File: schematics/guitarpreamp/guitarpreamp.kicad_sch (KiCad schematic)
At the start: 60 parts, among them J1 10k Pot, J2 Conn_01x07_Female, J3 Phones, Line Out, Line In, Mi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, U1 9V Linear Regulator, U2 TL074, U3 5V Linear Regulator, U4 3.3V Digital, U5 3.3V Analog, U6 WM8731SEDS, Y1 12.288MHz

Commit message: work on schematics
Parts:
- removed U2: TL074, symbol Amplifier_Operational:TL074
- added J4: Power Input, Connector_PinHeader_2.54mm:PinHeader_1x02_P2.54mm_Vertical, symbol Connector:Conn_01x02_Female
- added R19, R20: 10k, Resistor_SMD:R_0603_1608Metric_Pad0.98x0.95mm_HandSolder, symbol Device:R
- added U2: TL072, Package_SO:SOIC-8_3.9x4.9mm_P1.27mm, symbol Amplifier_Operational:TL072
- C1, C12, C13, C16, C17, C18, C19, C2, C22, C23, C24, C29, C3, C4, C5, C6, C7, C9: footprint (none) -> Capacitor_SMD:CP_Elec_4x4.5
- C10, C11: value ?pF -> 22pF; footprint (none) -> Capacitor_SMD:C_0603_1608Metric_Pad1.08x0.95mm_HandSolder
- C14, C15, C20, C21, C25: footprint (none) -> Capacitor_SMD:C_1210_3225Metric_Pad1.33x2.70mm_HandSolder
- C26, C27, C28, C8: footprint (none) -> Capacitor_SMD:C_0603_1608Metric_Pad1.08x0.95mm_HandSolder
- C30, C31: footprint (none) -> Capacitor_SMD:CP_Elec_6.3x7.7
- GuitarInput1: footprint (none) -> Connector_PinHeader_2.54mm:PinHeader_1x02_P2.54mm_Vertical
- J1: footprint (none) -> Connector_PinHeader_2.54mm:PinHeader_1x03_P2.54mm_Vertical
- J2: footprint (none) -> Connector_PinHeader_2.54mm:PinHeader_1x07_P2.54mm_Vertical
- J3: footprint (none) -> Connector_PinHeader_2.54mm:PinHeader_1x06_P2.54mm_Vertical
- R1, R10, R11, R12, R13, R14, R15, R16, R17, R18, R2, R3, R4, R5, R6, R7, R8, R9: footprint (none) -> Resistor_SMD:R_0603_1608Metric_Pad0.98x0.95mm_HandSolder
- U6: footprint Package_SO:SSOP-28_5.3x10.2mm_P0.65mm -> Package_DFN_QFN:QFN-28-1EP_5x5mm_P0.5mm_EP3.75x3.75mm
- Y1: footprint (none) -> Crystal:Crystal_SMD_HC49-SD_HandSoldering
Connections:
- net +12V: now also J4.2 (Pin_2)
- net +9V: now also U2.8 (V+)
- net GND: now also J4.1 (Pin_1), U2.4 (V-)
- net at C6.1, R4.1: now also U2.5 (+)
- net at C8.1, R3.2, R5.2: now also U2.6 (-)
- net at C8.2, C9.1, R5.1: now also U2.7
- net at C12.1, C13.1, C14.1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: now also R19.2, R20.2
- net at C5.1, R1.1, R2.2: now also U2.3 (+)
- net at R4.2: now also U2.1, U2.2 (-)
- net at J2.3 (Pin_3), U6.23 (SDIN): now also R19.1
- net at J2.2 (Pin_2), U6.24 (SCLK): now also R20.1
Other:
- moved on the sheet: C10, C11, C12, C13, C14, C15, C16, C17, C18, C19, C20, C21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

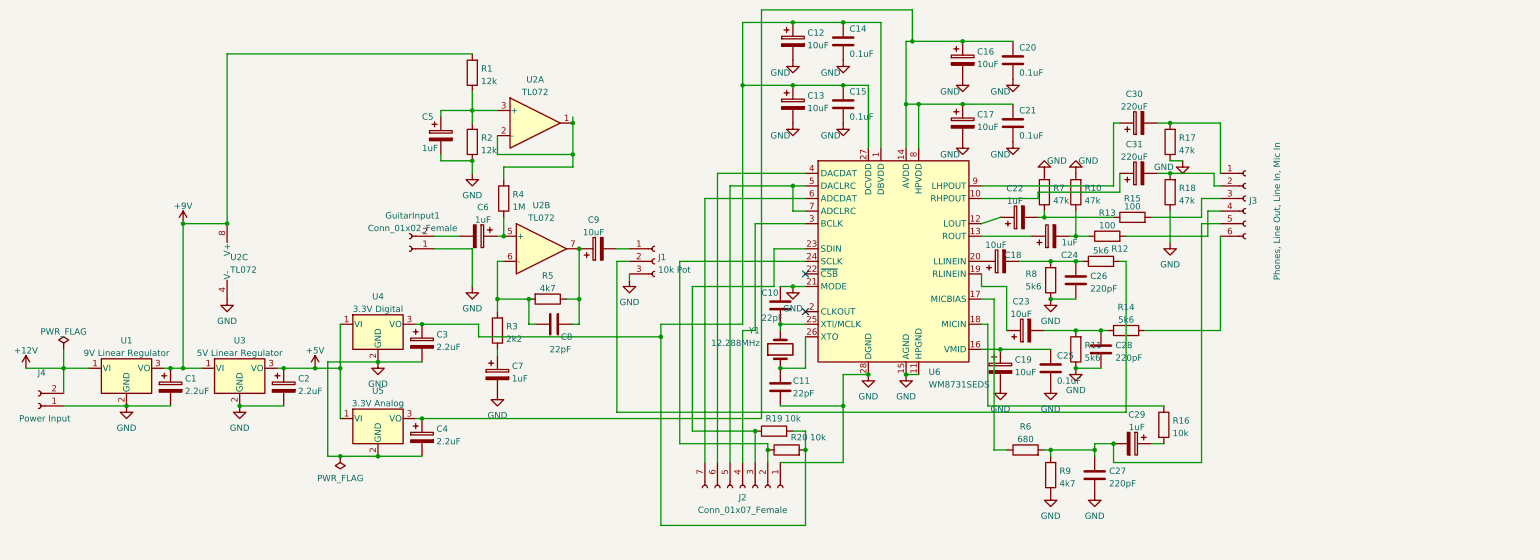
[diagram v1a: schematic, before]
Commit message: schematics
* moved fritzing schematics to schematics folder
* updated pcb
* adapted gitignore
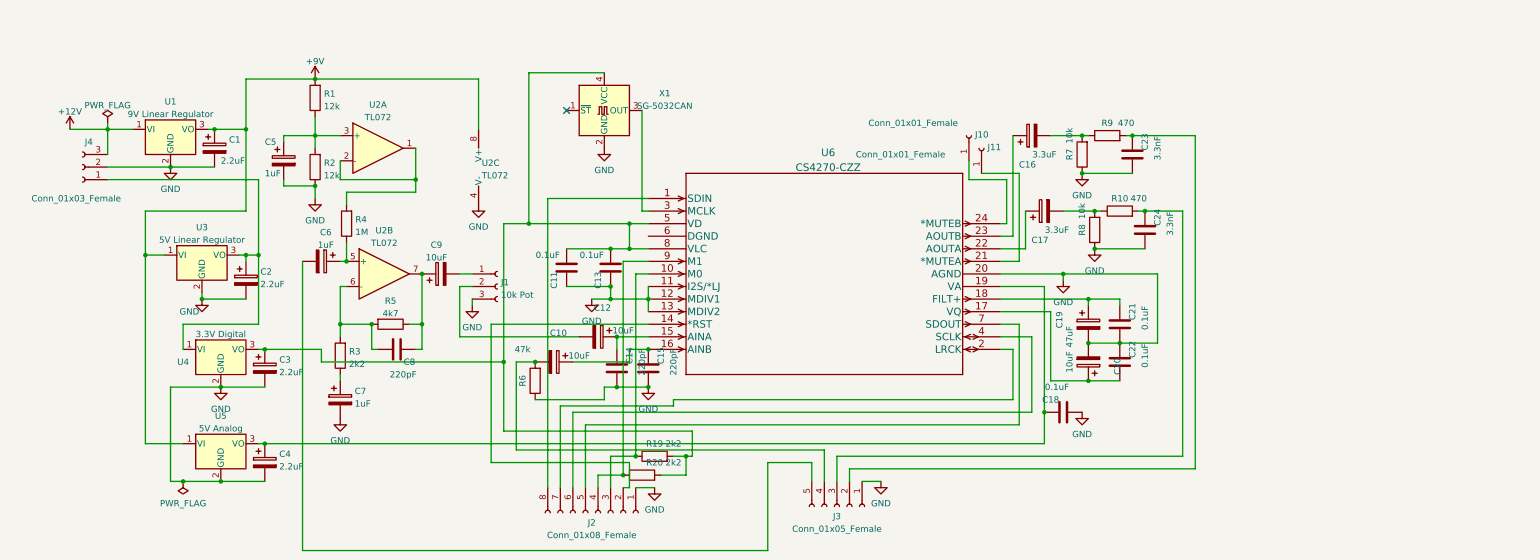
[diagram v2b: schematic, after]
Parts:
- removed C10: 22pF, Capacitor_SMD:C_0603_1608Metric_Pad1.08x0.95mm_HandSolder, symbol Device:C
- removed C13, C18, C23: 10uF, Capacitor_SMD:CP_Elec_4x4.5, symbol Device:C_Polarized
- removed C20, C25: 0.1uF, Capacitor_SMD:C_1210_3225Metric_Pad1.33x2.70mm_HandSolder, symbol Device:C
- removed C22, C24, C29: 1uF, Capacitor_SMD:CP_Elec_4x4.5, symbol Device:C_Polarized
- removed C26, C27, C28: 220pF, Capacitor_SMD:C_0603_1608Metric_Pad1.08x0.95mm_HandSolder, symbol Device:C
- removed C30, C31: 220uF, Capacitor_SMD:CP_Elec_6.3x7.7, symbol Device:C_Polarized
- removed GuitarInput1: Conn_01x02_Female, Connector_PinHeader_2.54mm:PinHeader_1x02_P2.54mm_Vertical, symbol Connector:Conn_01x02_Female
- removed J2: Conn_01x07_Female, Connector_PinHeader_2.54mm:PinHeader_1x07_P2.54mm_Vertical, symbol Connector:Conn_01x07_Female
- removed J3: Phones, Line Out, Line In, Mic In, Connector_PinHeader_2.54mm:PinHeader_1x06_P2.54mm_Vertical, symbol Connector:Conn_01x06_Female
- removed J4: Power Input, Connector_PinHeader_2.54mm:PinHeader_1x02_P2.54mm_Vertical, symbol Connector:Conn_01x02_Female
- removed R11, R12, R14: 5k6, Resistor_SMD:R_0603_1608Metric_Pad0.98x0.95mm_HandSolder, symbol Device:R
- removed R13, R15: 100, Resistor_SMD:R_0603_1608Metric_Pad0.98x0.95mm_HandSolder, symbol Device:R
- removed R16: 10k, Resistor_SMD:R_0603_1608Metric_Pad0.98x0.95mm_HandSolder, symbol Device:R
- removed R17, R18: 47k, Resistor_SMD:R_0603_1608Metric_Pad0.98x0.95mm_HandSolder, symbol Device:R
- removed U6: WM8731SEDS, Package_DFN_QFN:QFN-28-1EP_5x5mm_P0.5mm_EP3.75x3.75mm, symbol Audio:WM8731SEDS
- removed Y1: 12.288MHz, Crystal:Crystal_SMD_HC49-SD_HandSoldering, symbol Device:Crystal
- added C10, C20: 10uF, Capacitor_SMD:CP_Elec_4x4.5, symbol Device:C_Polarized
- added C13, C18, C22: 0.1uF, Capacitor_SMD:C_1210_3225Metric_Pad1.33x2.70mm_HandSolder, symbol Device:C
- added C23, C24: 3.3nF, Capacitor_SMD:C_0805_2012Metric_Pad1.18x1.45mm_HandSolder, symbol Device:C
- added J10, J11: Conn_01x01_Female, Connector_Pin:Pin_D0.7mm_L6.5mm_W1.8mm_FlatFork, symbol Connector:Conn_01x01_Female
- added J2: Conn_01x08_Female, Connector_PinHeader_2.54mm:PinHeader_1x08_P2.54mm_Vertical, symbol Connector:Conn_01x08_Female
- added J3: Conn_01x05_Female, Connector_PinHeader_2.54mm:PinHeader_1x05_P2.54mm_Vertical, symbol Connector:Conn_01x05_Female
- added J4: Conn_01x03_Female, Connector_PinHeader_2.54mm:PinHeader_1x03_P2.54mm_Vertical, symbol Connector:Conn_01x03_Female
- added U6: CS4270-CZZ, Package_SO:TSSOP-24_4.4x7.8mm_P0.65mm, symbol 2022-10-31_07-27-24:CS4270-CZZ
- added X1: SG-5032CAN, Oscillator:Oscillator_SMD_SeikoEpson_SG8002CA-4Pin_7.0x5.0mm_HandSoldering, symbol Oscillator:SG-5032CAN
- C11: value 22pF -> 0.1uF; footprint Capacitor_SMD:C_0603_1608Metric_Pad1.08x0.95mm_HandSolder -> Capacitor_SMD:C_1210_3225Metric_Pad1.33x2.70mm_HandSolder
- C14, C15: value 0.1uF -> 220pF; footprint Capacitor_SMD:C_1210_3225Metric_Pad1.33x2.70mm_HandSolder -> Capacitor_SMD:C_0603_1608Metric_Pad1.08x0.95mm_HandSolder
- C16, C17: value 10uF -> 3.3uF
- C19: value 10uF -> 47uF
- C8: value 22pF -> 220pF
- R10: value 47k -> 470
- R19, R20: value 10k -> 2k2
- R6: value 680 -> 47k
- R7: value 47k -> 10k
- R8: value 5k6 -> 10k
- R9: value 4k7 -> 470
- U4: footprint Package_TO_SOT_SMD:TO-252-2 -> Package_TO_SOT_SMD:TSOT-23-5_HandSoldering
- U5: value 3.3V Analog -> 5V Analog; footprint Package_TO_SOT_SMD:TO-252-2 -> Package_TO_SOT_SMD:TSOT-23-5_HandSoldering
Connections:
- net +12V: now also J4.3 (Pin_3)
- net +9V: now also U5.1 (VI)
- net GND: now also C14.1, C15.1, C21.1, R6.1, R7.1, C13.2, C18.1, C20.2, C22.2, C23.1, C24.1, J2.1 (Pin_1), J3.1 (Pin_1), J4.2 (Pin_2), U6.11 (I2S/*LJ), U6.12 (MDIV1), U6.13 (MDIV2), U6.20 (AGND), X1.2 (GND); no longer C12.2, C14.2, C15.2, C16.2, C17.2, C21.2, R10.2, R7.2, R9.1
- net at C11.1: now also C3.1, R19.2, R20.2, U4.3 (VO), C13.1, U6.5 (VD), U6.8 (VLC), X1.4 (VCC)
- net at R6.2: now also C10.2, J3.4 (Pin_4); no longer R9.2
- net at R10.1: now also C17.2, R8.2
- net at J1.2 (Pin_2): now also C12.2
- net at R20.1: now also J2.4 (Pin_4), U6.9 (M1)
- net at C6.2: now also J3.5 (Pin_5)
- net at C19.1: now also C21.2, U6.18 (FILT+)
- net at R19.1: now also J2.3 (Pin_3), U6.10 (M0)
- net +5V: no longer names the net of C2.1, U3.3 (VO), U4.1 (VI)
- net +5V: now also J4.1 (Pin_1); no longer U5.1 (VI)
- new net: C17.1, U6.22 (AOUTA)
- new net: C20.1, C22.1, U6.17 (VQ)
- new net: C12.1, C14.2, U6.15 (AINA)
- new net: C18.2, C4.1, U5.3 (VO), U6.19 (VA)
- new net: C24.2, J3.3 (Pin_3), R10.2
- new net: C10.1, C15.2, U6.16 (AINB)
- new net: J2.8 (Pin_8), U6.1 (SDIN)
- new net: J2.2 (Pin_2), U6.14 (*RST)
- new net: J2.7 (Pin_7), U6.2 (LRCK)
- new net: J11.1 (Pin_1), U6.21 (*MUTEA)
- new net: C16.1, U6.23 (AOUTB)
- new net: J10.1 (Pin_1), U6.24 (*MUTEB)
- new net: U6.3 (MCLK), X1.3 (OUT)
- new net: J2.6 (Pin_6), U6.4 (SCLK)
- new net: J2.5 (Pin_5), U6.7 (SDOUT)
- new net: C16.2, R7.2, R9.1
- new net: C23.2, J3.2 (Pin_2), R9.2
- no-connect marks 2 -> 1
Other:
- moved on the sheet: C1, C2, C3, C4, C5, C6, C7, C8, C9, J1, R1, R19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

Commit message: corrected some design mistakes
* connected oscillator enable to reset
* attached DGND
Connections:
- net GND: now also U6.6 (DGND)
- net at J2.2 (Pin_2), U6.14 (*RST): now also X1.1 (~{ST})
- no-connect marks 1 -> 0
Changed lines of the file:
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@@
   (junction (at 88.9 85.09) (diameter 0) (color 0 0 0 0)
   )
+  (junction (at 121.92 85.09) (diameter 0) (color 0 0 0 0)
+  )
   (junction (at 63.5 71.12) (diameter 0) (color 0 0 0 0)
   )
@@
   (junction (at 77.47 35.56) (diameter 0) (color 0 0 0 0)
   )
-  (no_connect (at 128.27 41.91))
   (wire (pts (xy 139.7 72.39) (xy 144.78 72.39))
     (stroke (width 0) (type default) (color 0 0 0 0))
@@
     (stroke (width 0) (type default) (color 0 0 0 0))
   )
+  (wire (pts (xy 134.62 67.31) (xy 144.78 67.31))
+    (stroke (width 0) (type default) (color 0 0 0 0))
+  )
   (wire (pts (xy 97.79 49.53) (xy 97.79 55.88))
     (stroke (width 0) (type default) (color 0 0 0 0))
@@
     (stroke (width 0) (type default) (color 0 0 0 0))
   )
+  (wire (pts (xy 121.92 41.91) (xy 121.92 85.09))
+    (stroke (width 0) (type default) (color 0 0 0 0))
+  )
   (wire (pts (xy 82.55 85.09) (xy 82.55 87.63))
     (stroke (width 0) (type default) (color 0 0 0 0))
@@
     (stroke (width 0) (type default) (color 0 0 0 0))
   )
+  (wire (pts (xy 121.92 85.09) (xy 144.78 85.09))
+    (stroke (width 0) (type default) (color 0 0 0 0))
+  )
   (wire (pts (xy 78.74 92.71) (xy 115.57 92.71))
     (stroke (width 0) (type default) (color 0 0 0 0))
@@
     (stroke (width 0) (type default) (color 0 0 0 0))
   )
-  (wire (pts (xy 113.03 85.09) (xy 144.78 85.09))
+  (wire (pts (xy 113.03 85.09) (xy 121.92 85.09))
     (stroke (width 0) (type default) (color 0 0 0 0))
   )
@@
   )
   (wire (pts (xy 63.5 45.72) (xy 63.5 35.56))
+    (stroke (width 0) (type default) (color 0 0 0 0))
+  )
+  (wire (pts (xy 128.27 41.91) (xy 121.92 41.91))
     (stroke (width 0) (type default) (color 0 0 0 0))
   )
@@
     (pin "2")
   )
+  (symbol (lib_id "power:GND") (at 134.62 67.31 270) (unit 1)
+    (in_bom yes) (on_board yes) (fields_autoplaced)
+    (property "Reference" "#PWR0116" (id 0) (at 128.27 67.31 0)
+      (effects (font (size 1.27 1.27)) hide)
+    )
+    (property "Value" "GND" (id 1) (at 131.4451 67.7438 90)
+      (effects (font (size 1.27 1.27)) (justify right))
+    )
+    (property "Footprint" "" (id 2) (at 134.62 67.31 0)
+      (effects (font (size 1.27 1.27)) hide)
+    )
+    (property "Datasheet" "" (id 3) (at 134.62 67.31 0)
+      (effects (font (size 1.27 1.27)) hide)
+    )
+    (pin "1")
+  )
   (symbol (lib_id "Device:R") (at 146.05 111.76 90) (unit 1)
     (in_bom yes) (on_board yes)
@@
       (reference "#PWR0115") (unit 1) (value "GND") (footprint "")
     )
+    (path "/957cba0c-9fde-4e24-888d-b1f289337beb"
+      (reference "#PWR0116") (unit 1) (value "GND") (footprint "")
+    )
     (path "/50a071a5-b567-4944-812b-66a65a33ff2d"

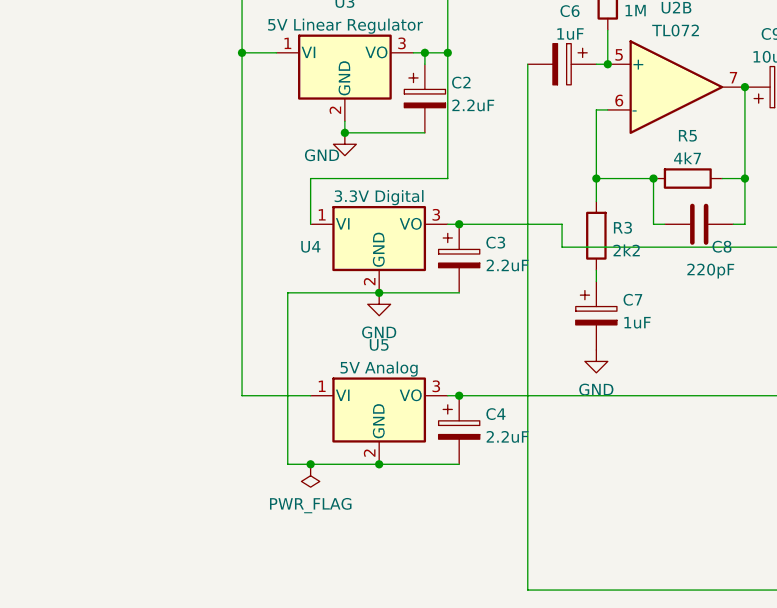
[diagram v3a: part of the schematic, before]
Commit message: changed regulators, added design fixes
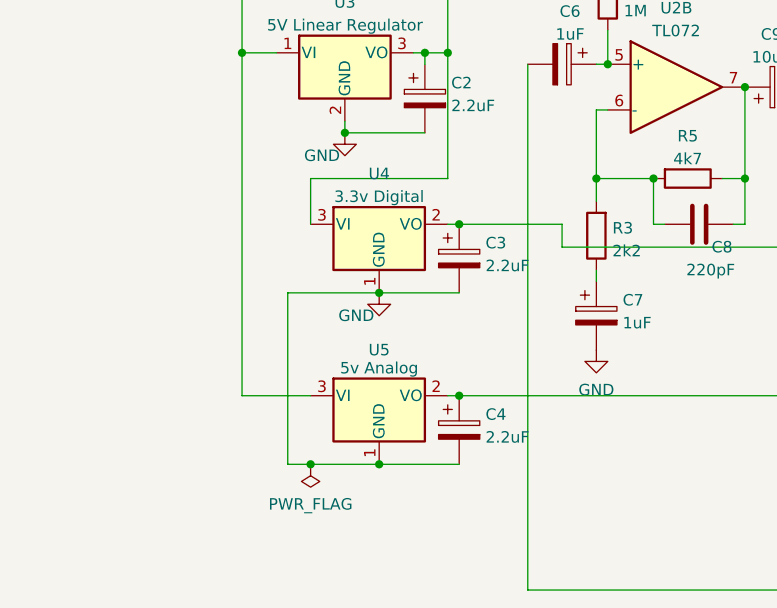
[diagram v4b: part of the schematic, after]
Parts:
- removed U4: 3.3V Digital, Package_TO_SOT_SMD:TSOT-23-5_HandSoldering, symbol Regulator_Linear:LM78M05_TO252
- removed U5: 5V Analog, Package_TO_SOT_SMD:TSOT-23-5_HandSoldering, symbol Regulator_Linear:LM78M05_TO252
- added U4: 3.3v Digital, Package_TO_SOT_SMD:SOT-23, symbol Regulator_Linear:MCP1700-1202E_SOT23
- added U5: 5v Analog, Package_TO_SOT_SMD:SOT-23, symbol Regulator_Linear:MCP1700-1202E_SOT23
- C19: footprint Capacitor_SMD:CP_Elec_4x4.5 -> Capacitor_SMD:CP_Elec_5x5.4
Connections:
- net +9V: now also U5.3 (VI)
- net GND: now also U4.1 (GND), U5.1 (GND)
- net at C18.2, C4.1, U6.19 (VA): now also U5.2 (VO)
- net at C11.1, C13.1, C3.1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: now also U4.2 (VO)
- net at C2.1, J4.1 (Pin_1), U3.3 (VO): now also U4.3 (VI)
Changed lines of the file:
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@@
 (kicad_sch (version 20211123) (generator eeschema)
   (paper "A4")
+  (junction (at 58.42 116.84) (diameter 0) (color 0 0 0 0)
+  )
   (junction (at 35.56 45.72) (diameter 0) (color 0 0 0 0)
   )
@@
   (junction (at 99.06 74.93) (diameter 0) (color 0 0 0 0)
   )
-  (junction (at 58.42 116.84) (diameter 0) (color 0 0 0 0)
-  )
   (junction (at 245.11 62.23) (diameter 0) (color 0 0 0 0)
   )
@@
     (stroke (width 0) (type default) (color 0 0 0 0))
   )
-  (wire (pts (xy 58.42 116.84) (xy 50.8 116.84))
+  (wire (pts (xy 50.8 116.84) (xy 58.42 116.84))
     (stroke (width 0) (type default) (color 0 0 0 0))
   )
@@
     (stroke (width 0) (type default) (color 0 0 0 0))
   )
+  (wire (pts (xy 58.42 116.84) (xy 67.31 116.84))
+    (stroke (width 0) (type default) (color 0 0 0 0))
+  )
   (wire (pts (xy 143.51 41.91) (xy 143.51 62.23))
     (stroke (width 0) (type default) (color 0 0 0 0))
@@
   )
   (wire (pts (xy 240.03 80.01) (xy 240.03 81.28))
-    (stroke (width 0) (type default) (color 0 0 0 0))
-  )
-  (wire (pts (xy 58.42 116.84) (xy 67.31 116.84))
     (stroke (width 0) (type default) (color 0 0 0 0))
   )
@@
     (pin "2")
   )
-  (symbol (lib_id "Regulator_Linear:LM78M05_TO252") (at 58.42 109.22 0) (unit 1)
-    (in_bom yes) (on_board yes) (fields_autoplaced)
-    (property "Reference" "U5" (id 0) (at 58.42 103.6152 0))
-    (property "Value" "5V Analog" (id 1) (at 58.42 106.1521 0))
-    (property "Footprint" "Package_TO_SOT_SMD:TSOT-23-5_HandSoldering" (id 2) (at 58.42 103.505 0)
-      (effects (font (size 1.27 1.27) italic) hide)
-    )
-    (property "Datasheet" "https://www.onsemi.com/pub/Collateral/MC78M00-D.PDF" (id 3) (at 58.42 110.49 0)
-      (effects (font (size 1.27 1.27)) hide)
-    )
-    (pin "1")
-    (pin "2")
-    (pin "3")
-  )
-  (symbol (lib_id "Regulator_Linear:LM78M05_TO252") (at 58.42 90.17 0) (unit 1)
-    (in_bom yes) (on_board yes)
-    (property "Reference" "U4" (id 0) (at 50.8 92.71 0))
-    (property "Value" "3.3V Digital" (id 1) (at 58.42 87.1021 0))
-    (property "Footprint" "Package_TO_SOT_SMD:TSOT-23-5_HandSoldering" (id 2) (at 58.42 84.455 0)
-      (effects (font (size 1.27 1.27) italic) hide)
-    )
-    (property "Datasheet" "https://www.onsemi.com/pub/Collateral/MC78M00-D.PDF" (id 3) (at 58.42 91.44 0)
-      (effects (font (size 1.27 1.27)) hide)
-    )
-    (pin "1")
-    (pin "2")
-    (pin "3")
-  )
   (symbol (lib_id "Device:C") (at 138.43 93.98 180) (unit 1)
     (in_bom yes) (on_board yes)
@@
     (pin "2")
   )
+  (symbol (lib_id "Regulator_Linear:MCP1700-1202E_SOT23") (at 58.42 90.17 0) (unit 1)
+    (in_bom yes) (on_board yes) (fields_autoplaced)
+    (property "Reference" "U4" (id 0) (at 58.42 84.5652 0))
+    (property "Value" "3.3v Digital" (id 1) (at 58.42 87.1021 0))
+    (property "Footprint" "Package_TO_SOT_SMD:SOT-23" (id 2) (at 58.42 84.455 0)
+      (effects (font (size 1.27 1.27)) hide)
+    )
+    (property "Datasheet" "http://ww1.microchip.com/downloads/en/DeviceDoc/20001826D.pdf" (id 3) (at 58.42 90.17 0)
+      (effects (font (size 1.27 1.27)) hide)
+    )
+    (pin "1")
+    (pin "2")
+    (pin "3")
+  )
   (symbol (lib_id "Device:C_Polarized") (at 125.73 92.71 270) (unit 1)
     (in_bom yes) (on_board yes)
@@
   )
   (symbol (lib_id "power:GND") (at 58.42 97.79 0) (unit 1)
-    (in_bom yes) (on_board yes) (fields_autoplaced)
+    (in_bom yes) (on_board yes)
     (property "Reference" "#PWR0101" (id 0) (at 58.42 104.14 0)
       (effects (font (size 1.27 1.27)) hide)
     )
-    (property "Value" "GND" (id 1) (at 58.42 102.2334 0))
+    (property "Value" "GND" (id 1) (at 55.88 100.33 0))
     (property "Footprint" "" (id 2) (at 58.42 97.79 0)
       (effects (font (size 1.27 1.27)) hide)
@@
     (pin "1")
   )
+  (symbol (lib_id "Regulator_Linear:MCP1700-1202E_SOT23") (at 58.42 109.22 0) (unit 1)
+    (in_bom yes) (on_board yes)
+    (property "Reference" "U5" (id 0) (at 58.42 104.14 0))
+    (property "Value" "5v Analog" (id 1) (at 58.42 106.1521 0))
+    (property "Footprint" "Package_TO_SOT_SMD:SOT-23" (id 2) (at 58.42 103.505 0)
+      (effects (font (size 1.27 1.27)) hide)
+    )
+    (property "Datasheet" "http://ww1.microchip.com/downloads/en/DeviceDoc/20001826D.pdf" (id 3) (at 58.42 109.22 0)
+      (effects (font (size 1.27 1.27)) hide)
+    )
+    (pin "1")
+    (pin "2")
+    (pin "3")
+  )
   (symbol (lib_id "power:PWR_FLAG") (at 35.56 44.45 0) (unit 1)
     (in_bom yes) (on_board yes) (fields_autoplaced)
@@
     (property "Reference" "C19" (id 0) (at 227.8212 84.201 90))
     (property "Value" "47uF" (id 1) (at 229.87 87.63 90))
-    (property "Footprint" "Capacitor_SMD:CP_Elec_4x4.5" (id 2) (at 234.6452 88.9 0)
+    (property "Footprint" "Capacitor_SMD:CP_Elec_5x5.4" (id 2) (at 234.6452 88.9 0)
       (effects (font (size 1.27 1.27)) hide)
     )
@@
     )
     (path "/a3ef7707-0ff1-4e68-a2d6-7b60ea11845e"
-      (reference "C19") (unit 1) (value "47uF") (footprint "Capacitor_SMD:CP_Elec_4x4.5")
+      (reference "C19") (unit 1) (value "47uF") (footprint "Capacitor_SMD:CP_Elec_5x5.4")
     )
     (path "/6ff48326-3bc9-4eb9-9e3d-c0cc30a5e536"
@@
       (reference "U3") (unit 1) (value "5V Linear Regulator") (footprint "Package_TO_SOT_SMD:TO-252-2")
     )
-    (path "/28db4465-0f4f-4a6b-8ffc-42b0f0137bf5"
-      (reference "U4") (unit 1) (value "3.3V Digital") (footprint "Package_TO_SOT_SMD:TSOT-23-5_HandSoldering")
-    )
-    (path "/21ab265f-0188-4037-aefc-ace4938bc6f0"
-      (reference "U5") (unit 1) (value "5V Analog") (footprint "Package_TO_SOT_SMD:TSOT-23-5_HandSoldering")
+    (path "/36a21b16-da19-4ec4-83c0-0c719498648d"
+      (reference "U4") (unit 1) (value "3.3v Digital") (footprint "Package_TO_SOT_SMD:SOT-23")
+    )
+    (path "/9fd3e1c5-af53-4f6b-9e3f-31908deb7985"
+      (reference "U5") (unit 1) (value "5v Analog") (footprint "Package_TO_SOT_SMD:SOT-23")
     )
     (path "/49e5bcdc-9f13-42ff-ad81-34f24b02cdcd"
